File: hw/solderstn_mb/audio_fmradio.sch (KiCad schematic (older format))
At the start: 39 parts, among them J2101 Conn_01x02, J2102 Molex_PicoBlade-53398-0271, J2103 Conn_01x02, J2104 Conn_01x02, U2101 Si4735-D60-GU, U2102 TS4990IDT, U2103 TS4990IDT

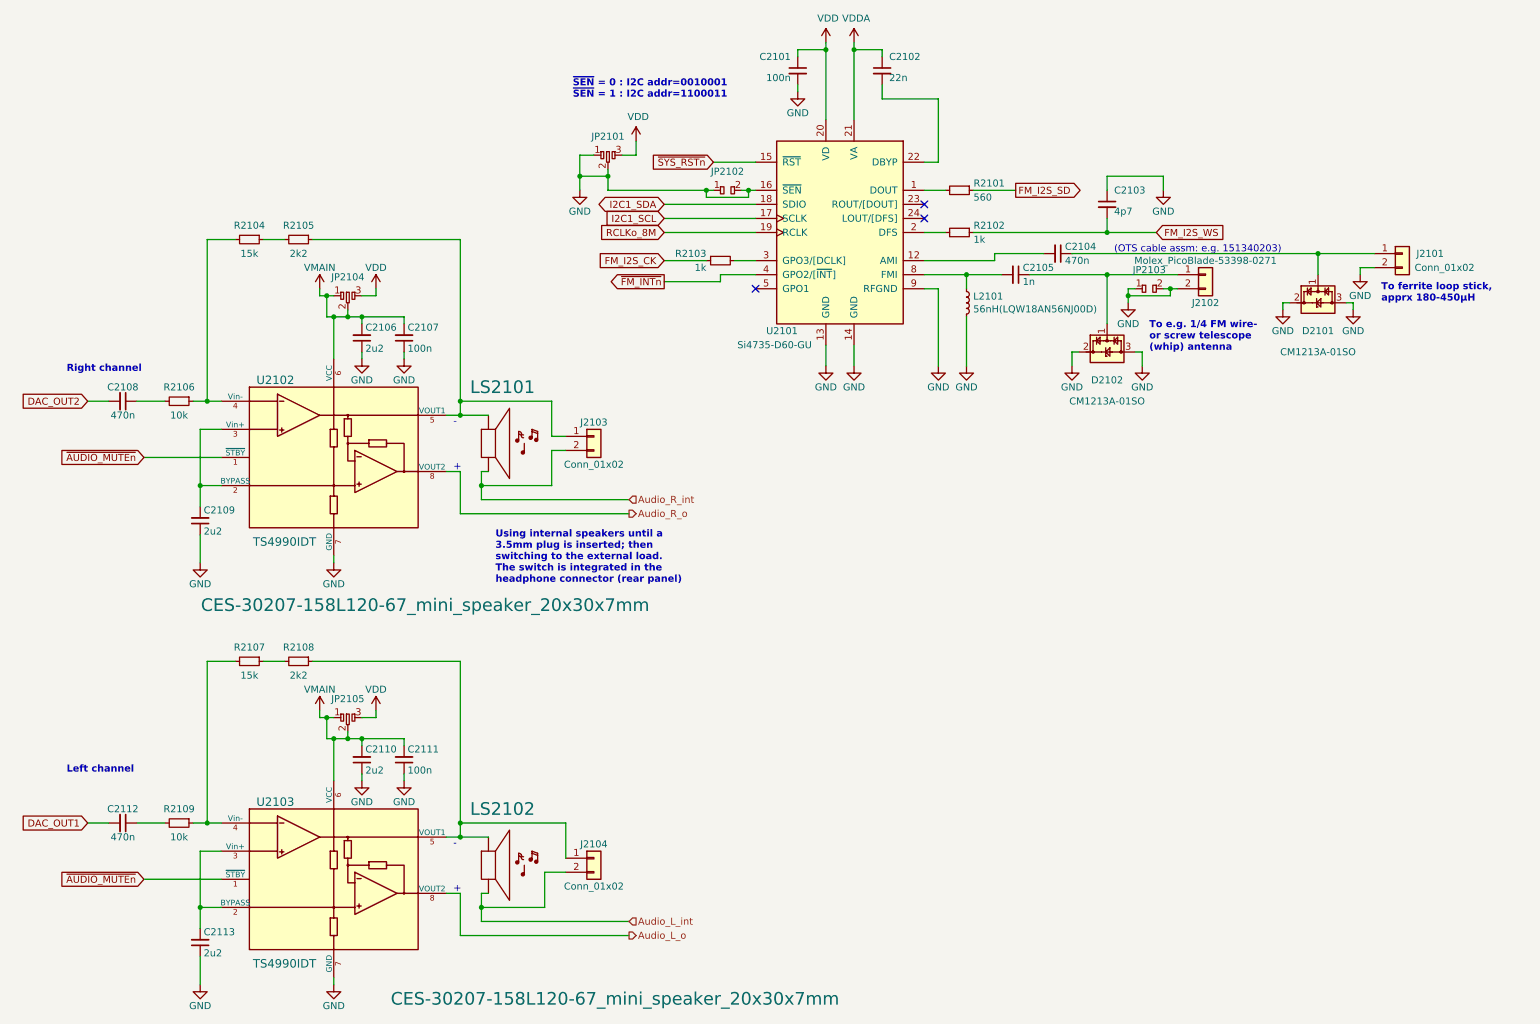
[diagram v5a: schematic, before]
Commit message: Updated MB audio to feature two alternative internal speakers; CUI CES-30207 or CES-703116 and their respective conn.headers. Speakers preliminary placed on MB top side
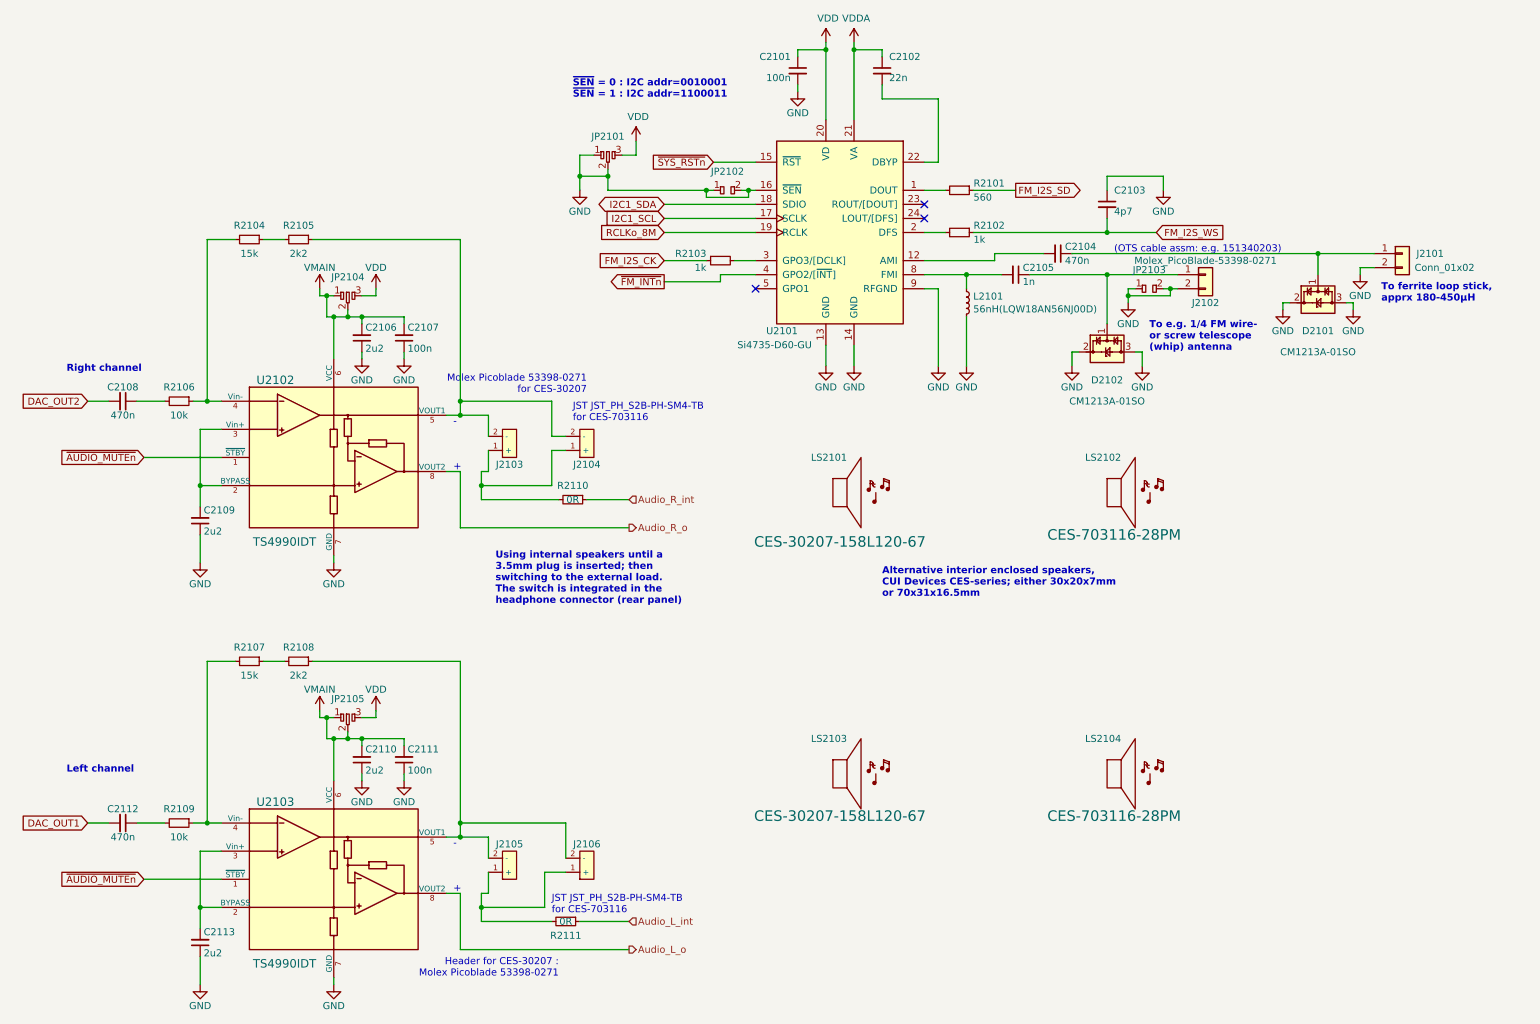
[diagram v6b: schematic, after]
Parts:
- removed J2103, J2104: Conn_01x02, Connector_PinHeader_2.54mm:PinHeader_1x02_P2.54mm_Vertical, symbol Connector_Generic:Conn_01x02
- removed LS2101, LS2102: CES-30207-158L120-67_mini_speaker_20x30x7mm, Connector_Molex:Molex_PicoBlade_53398-0271_1x02-1MP_P1.25mm_Vertical, symbol customlib_mj:CES-30207-158L120-67_mini_speaker_20x30x7mm
- added J2103, J2105: CES-30207-158L120-67_Molex-PicoBlade_conn, Connector_Molex:Molex_PicoBlade_53398-0271_1x02-1MP_P1.25mm_Vertical, symbol customlib_mj:CES-30207-158L120-67_Molex-PicoBlade_conn
- added J2104, J2106: CES-703116-28PM_JST-conn, Connector_JST:JST_PH_S2B-PH-SM4-TB_1x02-1MP_P2.00mm_Horizontal, symbol customlib_mj:CES-703116-28PM_JST-conn
- added LS2101, LS2103: CES-30207-158L120-67, customlib_mj_fp:CUI_CES-30207, symbol customlib_mj:CES-30207-158L120-67
- added LS2102, LS2104: CES-703116-28PM, customlib_mj_fp:CUI_CES-703116-28PM, symbol customlib_mj:CES-703116-28PM
- added R2110, R2111: 0R, Resistor_SMD:R_1206_3216Metric, symbol Device:R_Small
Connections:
- net Audio_L_int: now also R2111.1
- net Audio_R_int: now also R2110.1
- net at R2105.1, U2102.5 (VOUT1): now also J2103.2 (-), J2104.2 (-)
- net at R2108.1, U2103.5 (VOUT1): now also J2105.2 (-), J2106.2 (-)
- new net: J2103.1 (+), J2104.1 (+), R2110.2
- new net: J2105.1 (+), J2106.1 (+), R2111.2
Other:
- note added: "Alternative interior enclosed speakers,\nCUI Devices CES-series; either 30x20x7mm\nor 70x31x16.5mm"
- note added: "Header for CES-30207 :\nMolex Picoblade 53398-0271\n"
- note added: "JST JST_PH_S2B-PH-SM4-TB\nfor CES-703116"
- note added: "Molex Picoblade 53398-0271\nfor CES-30207"
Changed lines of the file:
@@
 	3700 3850 3800 3850
 Wire Wire Line
-	3800 3850 3800 4150
-Wire Wire Line
-	3800 4150 5000 4150
+	3800 3850 3800 4250
+Wire Wire Line
+	3800 4250 5000 4250
 Wire Wire Line
 	3700 6850 3800 6850
 Wire Wire Line
-	3800 6850 3800 7150
-Wire Wire Line
-	3800 7150 5000 7150
+	3800 6850 3800 7250
+Wire Wire Line
+	3800 7250 5000 7250
 Wire Wire Line
 	4000 6850 3950 6850
@@
 	3950 6850 3950 6950
 Wire Wire Line
-	3950 7050 5000 7050
-Wire Wire Line
 	4000 3850 3950 3850
 Wire Wire Line
 	3950 3850 3950 3950
-Wire Wire Line
-	3950 4050 5000 4050
 Text Notes 1000 6000 0    50   ~ 10
 Left channel
 Text Notes 1000 3150 0    50   ~ 10
 Right channel
-$Comp
-L Connector_Generic:Conn_01x02 J2103
-U 1 1 5F69C43E
-P 4750 3600
-F 0 "J2103" H 4750 3700 50  0000 C CNN
-F 1 "Conn_01x02" H 4750 3400 50  0000 C CNN
-F 2 "Connector_PinHeader_2.54mm:PinHeader_1x02_P2.54mm_Vertical" H 4750 3600 50  0001 C CNN
-F 3 "~" H 4750 3600 50  0001 C CNN
-	1    4750 3600
-	1    0    0    -1
-$EndComp
-$Comp
-L Connector_Generic:Conn_01x02 J2104
-U 1 1 5F69C9D9
-P 4750 6600
-F 0 "J2104" H 4750 6700 50  0000 C CNN
-F 1 "Conn_01x02" H 4750 6400 50  0000 C CNN
-F 2 "Connector_PinHeader_2.54mm:PinHeader_1x02_P2.54mm_Vertical" H 4750 6600 50  0001 C CNN
-F 3 "~" H 4750 6600 50  0001 C CNN
-	1    4750 6600
-	1    0    0    -1
-$EndComp
 Wire Wire Line
 	4550 6600 4550 6350
@@
 Wire Wire Line
 	3800 3350 3800 3450
-$Comp
-L customlib_mj:CES-30207-158L120-67_mini_speaker_20x30x7mm LS2102
-U 1 1 5F6F8808
-P 4000 6650
-F 0 "LS2102" H 4100 7050 90  0000 C CNN
-F 1 "CES-30207-158L120-67_mini_speaker_20x30x7mm" H 4900 5700 90  0000 C CNN
-F 2 "Connector_Molex:Molex_PicoBlade_53398-0271_1x02-1MP_P1.25mm_Vertical" H 4000 6650 90  0001 C CNN
-F 3 "https://www.cuidevices.com/product/audio/speakers/miniature-(10-mm~40-mm)/ces-30207-158l120-67" H 4000 6650 90  0001 C CNN
-	1    4000 6650
-	1    0    0    -1
-$EndComp
 Text Notes 3750 3850 0    50   ~ 0
 -\n\n\n\n+
@@
 Wire Wire Line
 	3400 6050 3400 6000
-Text Notes 4050 4650 0    50   ~ 10
+Text Notes 4050 4800 0    50   ~ 10
 Using internal speakers until a\n3.5mm plug is inserted; then\nswitching to the external load.\nThe switch is integrated in the\nheadphone connector (rear panel)
-Text HLabel 5000 4150 2    50   Output ~ 0
+Text HLabel 5000 4250 2    50   Output ~ 0
 Audio_R_o
-Text HLabel 5000 7150 2    50   Output ~ 0
+Text HLabel 5000 7250 2    50   Output ~ 0
 Audio_L_o
 Text HLabel 5000 4050 2    50   Input ~ 0
@@
 Text HLabel 5000 7050 2    50   Input ~ 0
 Audio_L_int
-$Comp
-L customlib_mj:CES-30207-158L120-67_mini_speaker_20x30x7mm LS2101
-U 1 1 5F6F74E3
-P 4000 3650
-F 0 "LS2101" H 4100 4050 90  0000 C CNN
-F 1 "CES-30207-158L120-67_mini_speaker_20x30x7mm" H 3550 2500 90  0000 C CNN
-F 2 "Connector_Molex:Molex_PicoBlade_53398-0271_1x02-1MP_P1.25mm_Vertical" H 4000 3650 90  0001 C CNN
-F 3 "https://www.cuidevices.com/product/audio/speakers/miniature-(10-mm~40-mm)/ces-30207-158l120-67" H 4000 3650 90  0001 C CNN
-	1    4000 3650
-	1    0    0    -1
-$EndComp
 Text Notes 8450 2300 0    50   ~ 0
 (OTS cable assm: e.g. 151340203)
@@
 Wire Wire Line
 	2850 5600 2900 5600
+Wire Wire Line
+	4000 3450 4000 3600
+Wire Wire Line
+	4000 3850 4000 3700
+Wire Wire Line
+	4000 6450 4000 6600
+Wire Wire Line
+	4000 6850 4000 6700
+Text Notes 4700 3300 2    50   ~ 0
+Molex Picoblade 53398-0271\nfor CES-30207
+Text Notes 4600 3500 0    50   ~ 0
+JST JST_PH_S2B-PH-SM4-TB\nfor CES-703116
+$Comp
+L customlib_mj:CES-30207-158L120-67_Molex-PicoBlade_conn J2103
+U 1 1 5F5CC286
+P 4150 3650
+F 0 "J2103" H 4150 3800 50  0000 C CNN
+F 1 "CES-30207-158L120-67_Molex-PicoBlade_conn" H 4150 3450 90  0001 C CNN
+F 2 "Connector_Molex:Molex_PicoBlade_53398-0271_1x02-1MP_P1.25mm_Vertical" H 4150 3300 90  0001 C CNN
+F 3 "https://www.molex.com/molex/products/part-detail/pcb_headers/0533980271" H 4150 3650 90  0001 C CNN
+	1    4150 3650
+	1    0    0    1
+$EndComp
+$Comp
+L customlib_mj:CES-30207-158L120-67_Molex-PicoBlade_conn J2105
+U 1 1 5F5CCC1E
+P 4150 6650
+F 0 "J2105" H 4150 6500 50  0000 C CNN
+F 1 "CES-30207-158L120-67_Molex-PicoBlade_conn" H 4150 6450 90  0001 C CNN
+F 2 "Connector_Molex:Molex_PicoBlade_53398-0271_1x02-1MP_P1.25mm_Vertical" H 4150 6300 90  0001 C CNN
+F 3 "https://www.molex.com/molex/products/part-detail/pcb_headers/0533980271" H 4150 6650 90  0001 C CNN
+	1    4150 6650
+	1    0    0    1
+$EndComp
+$Comp
+L customlib_mj:CES-703116-28PM_JST-conn J2106
+U 1 1 5F5D9839
+P 4700 6650
+F 0 "J2106" H 4700 6500 50  0000 C CNN
+F 1 "CES-703116-28PM_JST-conn" H 4700 6300 90  0001 C CNN
+F 2 "Connector_JST:JST_PH_S2B-PH-SM4-TB_1x02-1MP_P2.00mm_Horizontal" H 4700 6150 90  0001 C CNN
+F 3 "http://www.jst-mfg.com/product/pdf/eng/ePH.pdf?5f53c6b596f2a" H 4700 6650 90  0001 C CNN
+	1    4700 6650
+	1    0    0    1
+$EndComp
+$Comp
+L customlib_mj:CES-703116-28PM_JST-conn J2104
+U 1 1 5F5D9D8B
+P 4700 3650
+F 0 "J2104" H 4700 3800 50  0000 C CNN
+F 1 "CES-703116-28PM_JST-conn" H 4700 3300 90  0001 C CNN
+F 2 "Connector_JST:JST_PH_S2B-PH-SM4-TB_1x02-1MP_P2.00mm_Horizontal" H 4700 3150 90  0001 C CNN
+F 3 "http://www.jst-mfg.com/product/pdf/eng/ePH.pdf?5f53c6b596f2a" H 4700 3650 90  0001 C CNN
+	1    4700 3650
+	1    0    0    1
+$EndComp
+$Comp
+L customlib_mj:CES-30207-158L120-67 LS2101
+U 1 1 5F5E9E8B
+P 6500 4000
+F 0 "LS2101" H 6550 4250 50  0000 R CNN
+F 1 "CES-30207-158L120-67" H 6500 3650 75  0000 C CNN
+F 2 "customlib_mj_fp:CUI_CES-30207" H 6500 3600 50  0001 C CNN
+F 3 "https://www.cuidevices.com/product/audio/speakers/miniature-(10-mm~40-mm)/ces-30207-158l120-67" H 6500 4000 90  0001 C CNN
+	1    6500 4000
+	1    0    0    -1
+$EndComp
+$Comp
+L customlib_mj:CES-30207-158L120-67 LS2103
+U 1 1 5F5EA826
+P 6500 6000
+F 0 "LS2103" H 6550 6250 50  0000 R CNN
+F 1 "CES-30207-158L120-67" H 6500 5700 75  0000 C CNN
+F 2 "customlib_mj_fp:CUI_CES-30207" H 6500 5600 50  0001 C CNN
+F 3 "https://www.cuidevices.com/product/audio/speakers/miniature-(10-mm~40-mm)/ces-30207-158l120-67" H 6500 6000 90  0001 C CNN
+	1    6500 6000
+	1    0    0    -1
+$EndComp
+$Comp
+L customlib_mj:CES-703116-28PM LS2102
+U 1 1 5F5EB7EB
+P 8450 4000
+F 0 "LS2102" H 8500 4250 50  0000 R CNN
+F 1 "CES-703116-28PM" H 8450 3700 75  0000 C CNN
+F 2 "customlib_mj_fp:CUI_CES-703116-28PM" H 8600 3550 50  0001 C CNN
+F 3 "https://www.cuidevices.com/product/audio/speakers/standard-(41-mm~205-mm)/ces-703116-28pm" H 8450 4000 90  0001 C CNN
+	1    8450 4000
+	1    0    0    -1
+$EndComp
+$Comp
+L customlib_mj:CES-703116-28PM LS2104
+U 1 1 5F5EC280
+P 8450 6000
+F 0 "LS2104" H 8500 6250 50  0000 R CNN
+F 1 "CES-703116-28PM" H 8450 5700 75  0000 C CNN
+F 2 "customlib_mj_fp:CUI_CES-703116-28PM" H 8600 5550 50  0001 C CNN
+F 3 "https://www.cuidevices.com/product/audio/speakers/standard-(41-mm~205-mm)/ces-703116-28pm" H 8450 6000 90  0001 C CNN
+	1    8450 6000
+	1    0    0    -1
+$EndComp
+Text Notes 4500 7450 2    50   ~ 0
+Header for CES-30207 :\nMolex Picoblade 53398-0271\n
+Text Notes 4450 7000 0    50   ~ 0
+JST JST_PH_S2B-PH-SM4-TB\nfor CES-703116
+Text Notes 6800 4750 0    50   ~ 10
+Alternative interior enclosed speakers,\nCUI Devices CES-series; either 30x20x7mm\nor 70x31x16.5mm
+$Comp
+L Device:R_Small R2110
+U 1 1 5F5F9995
+P 4600 4050
+F 0 "R2110" V 4500 4050 50  0000 C CNN
+F 1 "0R" V 4600 4050 50  0000 C CNN
+F 2 "Resistor_SMD:R_1206_3216Metric" H 4600 4050 50  0001 C CNN
+F 3 "~" H 4600 4050 50  0001 C CNN
+	1    4600 4050
+	0    1    1    0
+$EndComp
+Wire Wire Line
+	4500 4050 3950 4050
+Wire Wire Line
+	4700 4050 5000 4050
+$Comp
+L Device:R_Small R2111
+U 1 1 5F620F17
+P 4550 7050
+F 0 "R2111" V 4650 7050 50  0000 C CNN
+F 1 "0R" V 4550 7050 50  0000 C CNN
+F 2 "Resistor_SMD:R_1206_3216Metric" H 4550 7050 50  0001 C CNN
+F 3 "~" H 4550 7050 50  0001 C CNN
+	1    4550 7050
+	0    1    1    0
+$EndComp
+Wire Wire Line
+	4650 7050 5000 7050
+Wire Wire Line
+	4450 7050 3950 7050
 $EndSCHEMATC

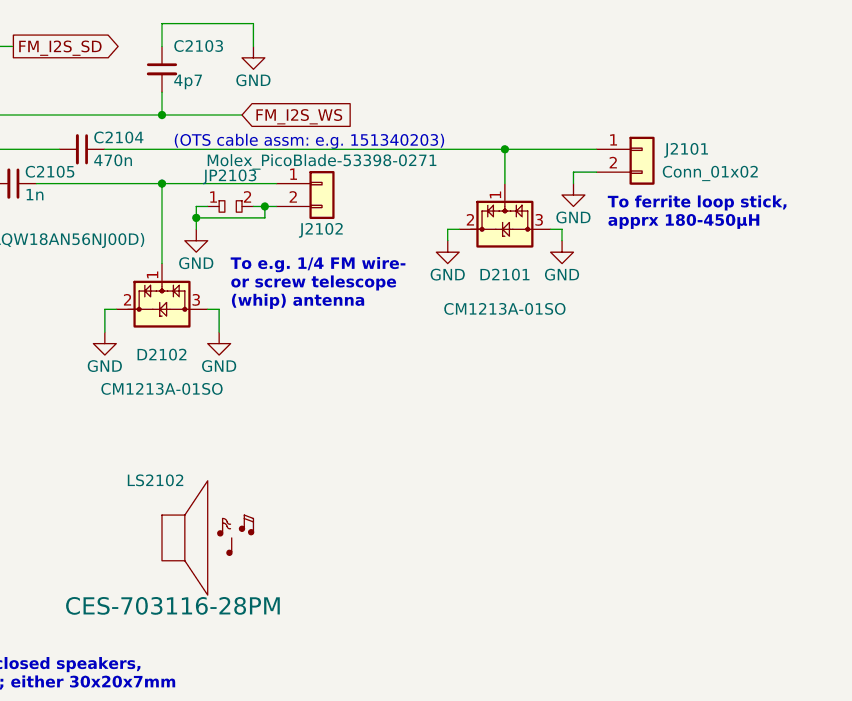
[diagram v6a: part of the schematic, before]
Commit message: Add 12V DC-out (Molex Nano-Fit 1x02) and SMA in back-panel, for FM antenna & ext. ant.amp. Updated Dsub9 conn to correct component & placement on MB.
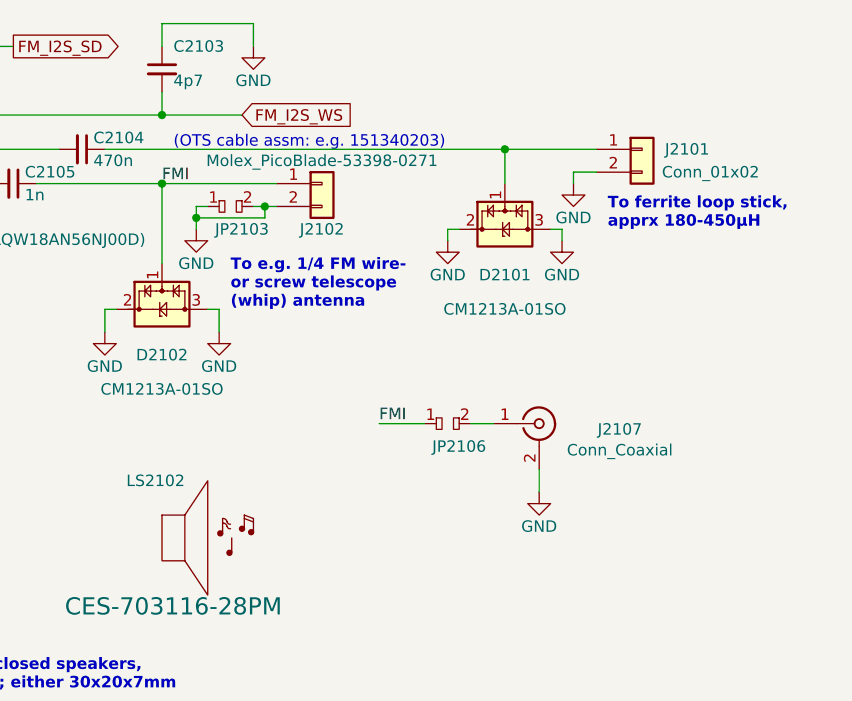
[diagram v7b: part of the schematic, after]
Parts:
- added J2107: Conn_Coaxial, customlib_mj_fp:SMA_Molex_73251-2200_Horizontal, symbol Connector:Conn_Coaxial
- added JP2106: dogbone_2_ud, customlib_mj_fp:db2_ud_0402, symbol customlib_mj:dogbone_2_ud
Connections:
- net GND: now also J2107.2 (Ext)
- net FMI: now reaches C2105.1, D2102.1 (CH1), J2102.1 (Pin_1)
- net FMI: now also JP2106.1
- new net: J2107.1 (In), JP2106.2
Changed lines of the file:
@@
 U 1 1 5F49CC1B
 P 8700 2550
-F 0 "JP2103" H 8700 2684 50  0000 C CNN
+F 0 "JP2103" H 8750 2450 50  0000 C CNN
 F 1 "dogbone_2_ud" H 8700 2650 50  0001 C CNN
 F 2 "customlib_mj_fp:db2_ud_0402" H 8700 2550 50  0001 C CNN
@@
 Wire Wire Line
 	4450 7050 3950 7050
+$Comp
+L Connector:Conn_Coaxial J2107
+U 1 1 5F81D28D
+P 10050 3500
+F 0 "J2107" H 10403 3475 50  0000 C CNN
+F 1 "Conn_Coaxial" H 10403 3384 50  0000 C CNN
+F 2 "customlib_mj_fp:SMA_Molex_73251-2200_Horizontal" H 10050 3500 50  0001 C CNN
+F 3 " ~" H 10050 3500 50  0001 C CNN
+	1    10050 3500
+	1    0    0    -1
+$EndComp
+$Comp
+L power:GND #PWR02129
+U 1 1 5F81D746
+P 10050 3800
+F 0 "#PWR02129" H 10050 3550 50  0001 C CNN
+F 1 "GND" H 10050 3650 50  0000 C CNN
+F 2 "" H 10050 3800 50  0001 C CNN
+F 3 "" H 10050 3800 50  0001 C CNN
+	1    10050 3800
+	1    0    0    -1
+$EndComp
+Wire Wire Line
+	10050 3800 10050 3700
+Text Label 8400 2450 0    50   ~ 0
+FMI
+Wire Wire Line
+	9850 3500 9750 3500
+Text Label 9350 3500 0    50   ~ 0
+FMI
+$Comp
+L customlib_mj:dogbone_2_ud JP2106
+U 1 1 5F832C0D
+P 9650 3500
+F 0 "JP2106" H 9700 3400 50  0000 C CNN
+F 1 "dogbone_2_ud" H 9650 3600 50  0001 C CNN
+F 2 "customlib_mj_fp:db2_ud_0402" H 9650 3500 50  0001 C CNN
+F 3 "" H 9650 3500 50  0001 C CNN
+	1    9650 3500
+	1    0    0    -1
+$EndComp
+Wire Wire Line
+	9550 3500 9350 3500
 $EndSCHEMATC

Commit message: *) Add some docs (JST PH spk conn., SPI-flash, Molex NanoFit 12V backpanel conn.) *) MB cutouts for front-panel features *) Change PwrBtn LED conn. Molex MicroClasp -> JST PH2 to avoid througholes + allow bottom-side fit above MW PSU *) Moving some stuff (RTC-module, connectors) due to collisions *) Fixed some components with broken 3d-packages
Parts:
- J2104, J2106: footprint Connector_JST:JST_PH_S2B-PH-SM4-TB_1x02-1MP_P2.00mm_Horizontal -> customlib_mj_fp:JST_PH_S2B-PH-SM4-TB_1x02-1MP_P2.00mm_Horizontal
- U2102, U2103: footprint Package_SO:SO-8_3.9x4.9mm_P1.27mm -> customlib_mj_fp:SOIC-8_3.9x4.9mm_P1.27mm
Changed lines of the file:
@@
 F 0 "U2102" H 2350 4300 60  0000 L CNN
 F 1 "TS4990IDT" H 2550 3150 60  0000 C CNN
-F 2 "Package_SO:SO-8_3.9x4.9mm_P1.27mm" H 2500 3550 60  0001 C CNN
+F 2 "customlib_mj_fp:SOIC-8_3.9x4.9mm_P1.27mm" H 2500 3550 60  0001 C CNN
 F 3 "" H 2500 3550 60  0001 C CNN
 	1    2900 3750
@@
 F 0 "U2103" H 2350 7300 60  0000 L CNN
 F 1 "TS4990IDT" H 2550 6150 60  0000 C CNN
-F 2 "Package_SO:SO-8_3.9x4.9mm_P1.27mm" H 2500 6550 60  0001 C CNN
+F 2 "customlib_mj_fp:SOIC-8_3.9x4.9mm_P1.27mm" H 2500 6550 60  0001 C CNN
 F 3 "" H 2500 6550 60  0001 C CNN
 	1    2900 6750
@@
 F 0 "J2106" H 4700 6500 50  0000 C CNN
 F 1 "CES-703116-28PM_JST-conn" H 4700 6300 90  0001 C CNN
-F 2 "Connector_JST:JST_PH_S2B-PH-SM4-TB_1x02-1MP_P2.00mm_Horizontal" H 4700 6150 90  0001 C CNN
+F 2 "customlib_mj_fp:JST_PH_S2B-PH-SM4-TB_1x02-1MP_P2.00mm_Horizontal" H 4700 6150 90  0001 C CNN
 F 3 "http://www.jst-mfg.com/product/pdf/eng/ePH.pdf?5f53c6b596f2a" H 4700 6650 90  0001 C CNN
 	1    4700 6650
@@
 F 0 "J2104" H 4700 3800 50  0000 C CNN
 F 1 "CES-703116-28PM_JST-conn" H 4700 3300 90  0001 C CNN
-F 2 "Connector_JST:JST_PH_S2B-PH-SM4-TB_1x02-1MP_P2.00mm_Horizontal" H 4700 3150 90  0001 C CNN
+F 2 "customlib_mj_fp:JST_PH_S2B-PH-SM4-TB_1x02-1MP_P2.00mm_Horizontal" H 4700 3150 90  0001 C CNN
 F 3 "http://www.jst-mfg.com/product/pdf/eng/ePH.pdf?5f53c6b596f2a" H 4700 3650 90  0001 C CNN
 	1    4700 3650
